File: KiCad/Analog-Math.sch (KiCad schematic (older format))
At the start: 13 parts, among them Q19 2N3904

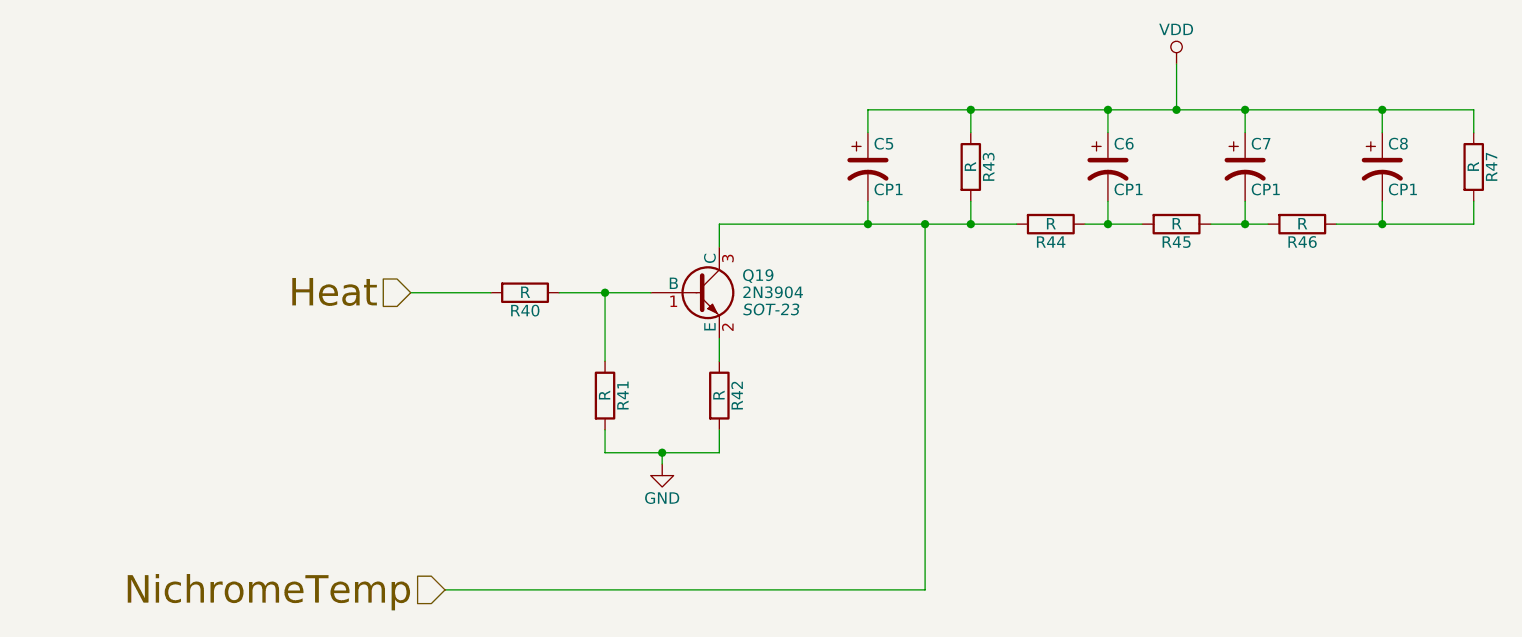
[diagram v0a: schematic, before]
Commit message: HeatOn fix, replaced R1-8 with array
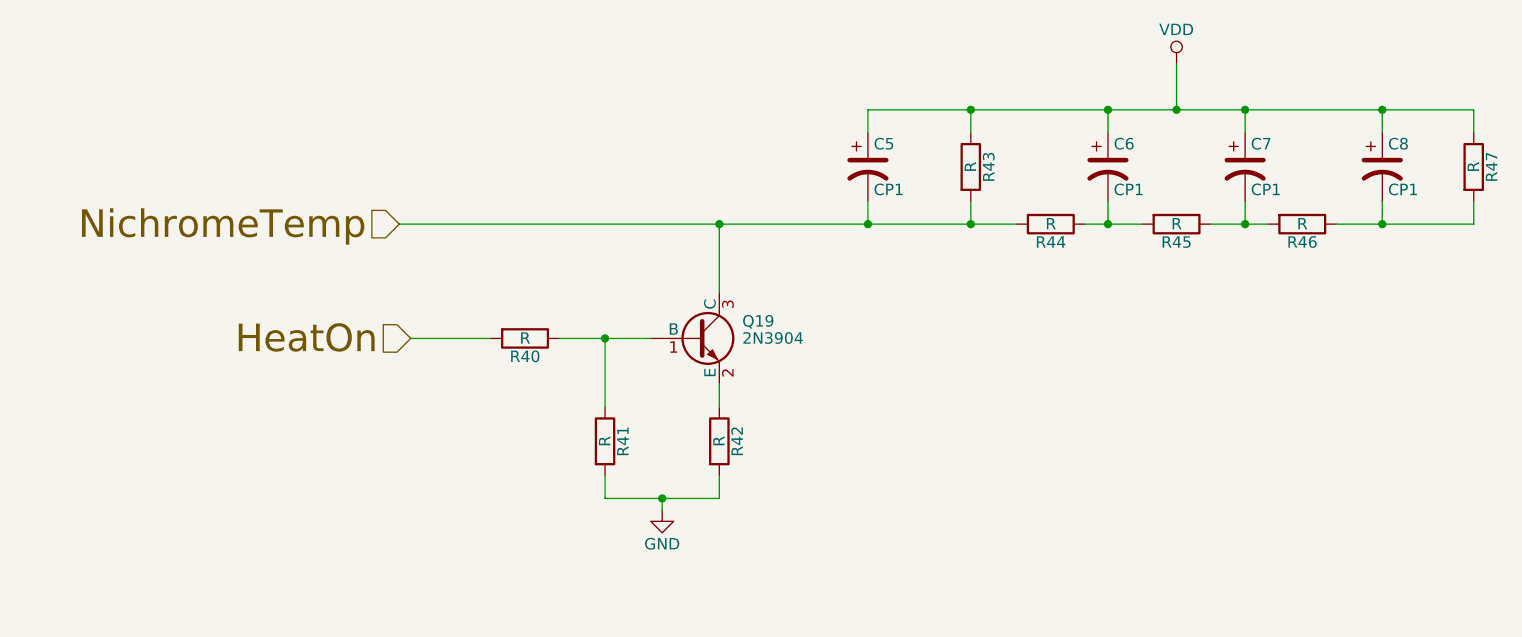
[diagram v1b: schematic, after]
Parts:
- Q19: footprint SOT-23 -> (none)
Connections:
- net Heat renamed HeatOn
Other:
- moved on the sheet: Q19, R40, R41, R42
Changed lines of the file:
@@
 Comment4 ""
 $EndDescr
-Text HLabel 3000 4200 0    120  Input ~ 0
+Text HLabel 2800 2600 0    120  Input ~ 0
 NichromeTemp
-Text HLabel 2850 2900 0    120  Input ~ 0
-Heat
+Text HLabel 2850 3100 0    120  Input ~ 0
+HeatOn
 $Comp
 L MMBT3904 Q19
 U 1 1 5683E9CB
-P 4100 2900
-F 0 "Q19" H 4300 2975 50  0000 L CNN
-F 1 "2N3904" H 4300 2900 50  0000 L CNN
-F 2 "SOT-23" H 4300 2825 50  0000 L CIN
-F 3 "" H 4100 2900 50  0000 L CNN
-	1    4100 2900
+P 4100 3100
+F 0 "Q19" H 4300 3175 50  0000 L CNN
+F 1 "2N3904" H 4300 3100 50  0000 L CNN
+F 2 "" H 4300 3025 50  0001 L CIN
+F 3 "" H 4100 3100 50  0000 L CNN
+	1    4100 3100
 	1    0    0    -1
 $EndComp
@@
 L R R40
 U 1 1 5683EA71
-P 3350 2900
-F 0 "R40" V 3430 2900 50  0000 C CNN
-F 1 "R" V 3350 2900 50  0000 C CNN
-F 2 "" V 3280 2900 50  0000 C CNN
-F 3 "" H 3350 2900 50  0000 C CNN
-	1    3350 2900
+P 3350 3100
+F 0 "R40" V 3430 3100 50  0000 C CNN
+F 1 "R" V 3350 3100 50  0000 C CNN
+F 2 "" V 3280 3100 50  0001 C CNN
+F 3 "" H 3350 3100 50  0000 C CNN
+	1    3350 3100
 	0    1    1    0
 $EndComp
@@
 L R R41
 U 1 1 5683EABC
-P 3700 3350
-F 0 "R41" V 3780 3350 50  0000 C CNN
-F 1 "R" V 3700 3350 50  0000 C CNN
-F 2 "" V 3630 3350 50  0000 C CNN
-F 3 "" H 3700 3350 50  0000 C CNN
-	1    3700 3350
+P 3700 3550
+F 0 "R41" V 3780 3550 50  0000 C CNN
+F 1 "R" V 3700 3550 50  0000 C CNN
+F 2 "" V 3630 3550 50  0001 C CNN
+F 3 "" H 3700 3550 50  0000 C CNN
+	1    3700 3550
 	1    0    0    -1
 $EndComp
@@
 L R R42
 U 1 1 5683ED88
-P 4200 3350
-F 0 "R42" V 4280 3350 50  0000 C CNN
-F 1 "R" V 4200 3350 50  0000 C CNN
-F 2 "" V 4130 3350 50  0000 C CNN
-F 3 "" H 4200 3350 50  0000 C CNN
-	1    4200 3350
-	1    0    0    -1
-$EndComp
-$Comp
-L GND #PWR48
+P 4200 3550
+F 0 "R42" V 4280 3550 50  0000 C CNN
+F 1 "R" V 4200 3550 50  0000 C CNN
+F 2 "" V 4130 3550 50  0001 C CNN
+F 3 "" H 4200 3550 50  0000 C CNN
+	1    4200 3550
+	1    0    0    -1
+$EndComp
+$Comp
+L GND #PWR048
 U 1 1 5683EDA5
-P 3950 3650
-F 0 "#PWR48" H 3950 3400 50  0001 C CNN
-F 1 "GND" H 3950 3500 50  0000 C CNN
-F 2 "" H 3950 3650 50  0000 C CNN
-F 3 "" H 3950 3650 50  0000 C CNN
-	1    3950 3650
+P 3950 3850
+F 0 "#PWR048" H 3950 3600 50  0001 C CNN
+F 1 "GND" H 3950 3700 50  0000 C CNN
+F 2 "" H 3950 3850 50  0000 C CNN
+F 3 "" H 3950 3850 50  0000 C CNN
+	1    3950 3850
 	1    0    0    -1
 $EndComp
@@
 F 0 "C5" H 4875 2450 50  0000 L CNN
 F 1 "CP1" H 4875 2250 50  0000 L CNN
-F 2 "" H 4850 2350 50  0000 C CNN
+F 2 "" H 4850 2350 50  0001 C CNN
 F 3 "" H 4850 2350 50  0000 C CNN
 	1    4850 2350
@@
 $EndComp
 $Comp
-L VDD #PWR49
+L VDD #PWR049
 U 1 1 5683F0D4
 P 6200 1900
-F 0 "#PWR49" H 6200 1750 50  0001 C CNN
+F 0 "#PWR049" H 6200 1750 50  0001 C CNN
 F 1 "VDD" H 6200 2050 50  0000 C CNN
 F 2 "" H 6200 1900 50  0000 C CNN
@@
 $EndComp
 Wire Wire Line
-	2850 2900 3200 2900
-Wire Wire Line
-	3500 2900 3900 2900
-Wire Wire Line
-	3700 2900 3700 3200
-Connection ~ 3700 2900
-Wire Wire Line
-	3700 3500 3700 3600
-Wire Wire Line
-	3700 3600 4200 3600
-Wire Wire Line
-	4200 3600 4200 3500
-Wire Wire Line
-	4200 3200 4200 3100
-Wire Wire Line
-	3950 3650 3950 3600
-Connection ~ 3950 3600
-Wire Wire Line
-	4200 2700 4200 2600
+	2850 3100 3200 3100
+Wire Wire Line
+	3500 3100 3900 3100
+Wire Wire Line
+	3700 3100 3700 3400
+Connection ~ 3700 3100
+Wire Wire Line
+	3700 3700 3700 3800
+Wire Wire Line
+	3700 3800 4200 3800
+Wire Wire Line
+	4200 3800 4200 3700
+Wire Wire Line
+	4200 3400 4200 3300
+Wire Wire Line
+	3950 3850 3950 3800
+Connection ~ 3950 3800
+Wire Wire Line
+	4200 2600 4200 2900
 Wire Wire Line
 	4850 2600 4850 2500
@@
 F 0 "R43" V 5380 2350 50  0000 C CNN
 F 1 "R" V 5300 2350 50  0000 C CNN
-F 2 "" V 5230 2350 50  0000 C CNN
+F 2 "" V 5230 2350 50  0001 C CNN
 F 3 "" H 5300 2350 50  0000 C CNN
 	1    5300 2350
@@
 F 0 "R44" V 5730 2600 50  0000 C CNN
 F 1 "R" V 5650 2600 50  0000 C CNN
-F 2 "" V 5580 2600 50  0000 C CNN
+F 2 "" V 5580 2600 50  0001 C CNN
 F 3 "" H 5650 2600 50  0000 C CNN
 	1    5650 2600
@@
 F 0 "R46" V 6830 2600 50  0000 C CNN
 F 1 "R" V 6750 2600 50  0000 C CNN
-F 2 "" V 6680 2600 50  0000 C CNN
+F 2 "" V 6680 2600 50  0001 C CNN
 F 3 "" H 6750 2600 50  0000 C CNN
 	1    6750 2600
@@
 F 0 "C8" H 7125 2450 50  0000 L CNN
 F 1 "CP1" H 7125 2250 50  0000 L CNN
-F 2 "" H 7100 2350 50  0000 C CNN
+F 2 "" H 7100 2350 50  0001 C CNN
 F 3 "" H 7100 2350 50  0000 C CNN
 	1    7100 2350
@@
 F 0 "R47" V 7580 2350 50  0000 C CNN
 F 1 "R" V 7500 2350 50  0000 C CNN
-F 2 "" V 7430 2350 50  0000 C CNN
+F 2 "" V 7430 2350 50  0001 C CNN
 F 3 "" H 7500 2350 50  0000 C CNN
 	1    7500 2350
@@
 	6200 1900 6200 2100
 Connection ~ 6200 2100
-Wire Wire Line
-	5100 2600 5100 4200
-Wire Wire Line
-	5100 4200 3000 4200
 $Comp
 L R R45
@@
 F 0 "R45" V 6280 2600 50  0000 C CNN
 F 1 "R" V 6200 2600 50  0000 C CNN
-F 2 "" V 6130 2600 50  0000 C CNN
+F 2 "" V 6130 2600 50  0001 C CNN
 F 3 "" H 6200 2600 50  0000 C CNN
 	1    6200 2600
@@
 F 0 "C6" H 5925 2450 50  0000 L CNN
 F 1 "CP1" H 5925 2250 50  0000 L CNN
-F 2 "" H 5900 2350 50  0000 C CNN
+F 2 "" H 5900 2350 50  0001 C CNN
 F 3 "" H 5900 2350 50  0000 C CNN
 	1    5900 2350
@@
 F 0 "C7" H 6525 2450 50  0000 L CNN
 F 1 "CP1" H 6525 2250 50  0000 L CNN
-F 2 "" H 6500 2350 50  0000 C CNN
+F 2 "" H 6500 2350 50  0001 C CNN
 F 3 "" H 6500 2350 50  0000 C CNN
 	1    6500 2350
@@
 $EndComp
 Wire Wire Line
-	4200 2600 5500 2600
-Connection ~ 5100 2600
+	2800 2600 5500 2600
 Connection ~ 5300 2600
 Wire Wire Line
@@
 Connection ~ 7100 2600
 Connection ~ 4850 2600
+Connection ~ 4200 2600
 $EndSCHEMATC

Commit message: kicad resistor package associations complete
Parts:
- R40, R41, R42, R43, R44, R45, R46, R47: footprint (none) -> Resistors_ThroughHole:Resistor_Horizontal_RM10mm
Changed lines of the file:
@@
 F 0 "R40" V 3430 3100 50  0000 C CNN
 F 1 "R" V 3350 3100 50  0000 C CNN
-F 2 "" V 3280 3100 50  0001 C CNN
+F 2 "Resistors_ThroughHole:Resistor_Horizontal_RM10mm" V 3280 3100 50  0001 C CNN
 F 3 "" H 3350 3100 50  0000 C CNN
 	1    3350 3100
@@
 F 0 "R41" V 3780 3550 50  0000 C CNN
 F 1 "R" V 3700 3550 50  0000 C CNN
-F 2 "" V 3630 3550 50  0001 C CNN
+F 2 "Resistors_ThroughHole:Resistor_Horizontal_RM10mm" V 3630 3550 50  0001 C CNN
 F 3 "" H 3700 3550 50  0000 C CNN
 	1    3700 3550
@@
 F 0 "R42" V 4280 3550 50  0000 C CNN
 F 1 "R" V 4200 3550 50  0000 C CNN
-F 2 "" V 4130 3550 50  0001 C CNN
+F 2 "Resistors_ThroughHole:Resistor_Horizontal_RM10mm" V 4130 3550 50  0001 C CNN
 F 3 "" H 4200 3550 50  0000 C CNN
 	1    4200 3550
@@
 F 0 "R43" V 5380 2350 50  0000 C CNN
 F 1 "R" V 5300 2350 50  0000 C CNN
-F 2 "" V 5230 2350 50  0001 C CNN
+F 2 "Resistors_ThroughHole:Resistor_Horizontal_RM10mm" V 5230 2350 50  0001 C CNN
 F 3 "" H 5300 2350 50  0000 C CNN
 	1    5300 2350
@@
 F 0 "R44" V 5730 2600 50  0000 C CNN
 F 1 "R" V 5650 2600 50  0000 C CNN
-F 2 "" V 5580 2600 50  0001 C CNN
+F 2 "Resistors_ThroughHole:Resistor_Horizontal_RM10mm" V 5580 2600 50  0001 C CNN
 F 3 "" H 5650 2600 50  0000 C CNN
 	1    5650 2600
@@
 F 0 "R46" V 6830 2600 50  0000 C CNN
 F 1 "R" V 6750 2600 50  0000 C CNN
-F 2 "" V 6680 2600 50  0001 C CNN
+F 2 "Resistors_ThroughHole:Resistor_Horizontal_RM10mm" V 6680 2600 50  0001 C CNN
 F 3 "" H 6750 2600 50  0000 C CNN
 	1    6750 2600
@@
 F 0 "R47" V 7580 2350 50  0000 C CNN
 F 1 "R" V 7500 2350 50  0000 C CNN
-F 2 "" V 7430 2350 50  0001 C CNN
+F 2 "Resistors_ThroughHole:Resistor_Horizontal_RM10mm" V 7430 2350 50  0001 C CNN
 F 3 "" H 7500 2350 50  0000 C CNN
 	1    7500 2350
@@
 F 0 "R45" V 6280 2600 50  0000 C CNN
 F 1 "R" V 6200 2600 50  0000 C CNN
-F 2 "" V 6130 2600 50  0001 C CNN
+F 2 "Resistors_ThroughHole:Resistor_Horizontal_RM10mm" V 6130 2600 50  0001 C CNN
 F 3 "" H 6200 2600 50  0000 C CNN
 	1    6200 2600

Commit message: capacitors and diode part associations
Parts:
- C5, C6, C7, C8: footprint (none) -> Capacitors_ThroughHole:C_Disc_D6_P5
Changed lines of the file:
@@
 F 0 "C5" H 4875 2450 50  0000 L CNN
 F 1 "CP1" H 4875 2250 50  0000 L CNN
-F 2 "" H 4850 2350 50  0001 C CNN
+F 2 "Capacitors_ThroughHole:C_Disc_D6_P5" H 4850 2350 50  0001 C CNN
 F 3 "" H 4850 2350 50  0000 C CNN
 	1    4850 2350
@@
 F 0 "C8" H 7125 2450 50  0000 L CNN
 F 1 "CP1" H 7125 2250 50  0000 L CNN
-F 2 "" H 7100 2350 50  0001 C CNN
+F 2 "Capacitors_ThroughHole:C_Disc_D6_P5" H 7100 2350 50  0001 C CNN
 F 3 "" H 7100 2350 50  0000 C CNN
 	1    7100 2350
@@
 F 0 "C6" H 5925 2450 50  0000 L CNN
 F 1 "CP1" H 5925 2250 50  0000 L CNN
-F 2 "" H 5900 2350 50  0001 C CNN
+F 2 "Capacitors_ThroughHole:C_Disc_D6_P5" H 5900 2350 50  0001 C CNN
 F 3 "" H 5900 2350 50  0000 C CNN
 	1    5900 2350
@@
 F 0 "C7" H 6525 2450 50  0000 L CNN
 F 1 "CP1" H 6525 2250 50  0000 L CNN
-F 2 "" H 6500 2350 50  0001 C CNN
+F 2 "Capacitors_ThroughHole:C_Disc_D6_P5" H 6500 2350 50  0001 C CNN
 F 3 "" H 6500 2350 50  0000 C CNN
 	1    6500 2350

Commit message: IC BOM and footprints complete
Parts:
- removed Q19: 2N3904, symbol MMBT3904
- added Q19: 2N3904, Easy-PCB-footprints:TO-92, symbol 2N3904
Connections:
- net NichromeTemp: now also Q19.3 (C)
- net at R40.1, R41.1: now also Q19.2 (B)
- net at R42.1: now also Q19.1 (E)
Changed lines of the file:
@@
 HeatOn
-$Comp
-L MMBT3904 Q19
-U 1 1 5683E9CB
-P 4100 3100
-F 0 "Q19" H 4300 3175 50  0000 L CNN
-F 1 "2N3904" H 4300 3100 50  0000 L CNN
-F 2 "" H 4300 3025 50  0001 L CIN
-F 3 "" H 4100 3100 50  0000 L CNN
-	1    4100 3100
-	1    0    0    -1
-$EndComp
 $Comp
 L R R40
@@
 Connection ~ 4850 2600
 Connection ~ 4200 2600
+$Comp
+L 2N3904 Q19
+U 1 1 56882825
+P 4100 3100
+F 0 "Q19" H 4300 3175 50  0000 L CNN
+F 1 "2N3904" H 4300 3100 50  0000 L CNN
+F 2 "Easy-PCB-footprints:TO-92" H 4300 3025 50  0000 L CIN
+F 3 "" H 4100 3100 50  0000 L CNN
+	1    4100 3100
+	1    0    0    -1
+$EndComp
 $EndSCHEMATC

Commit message: errors cleared and components on board
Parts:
- C5, C6, C7, C8: footprint Capacitors_ThroughHole:C_Disc_D6_P5 -> Easy-PCB-footprints:C_Disc_D6_P5
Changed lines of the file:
@@
 F 0 "C5" H 4875 2450 50  0000 L CNN
 F 1 "CP1" H 4875 2250 50  0000 L CNN
-F 2 "Capacitors_ThroughHole:C_Disc_D6_P5" H 4850 2350 50  0001 C CNN
+F 2 "Easy-PCB-footprints:C_Disc_D6_P5" H 4850 2350 50  0001 C CNN
 F 3 "" H 4850 2350 50  0000 C CNN
 	1    4850 2350
@@
 F 0 "C8" H 7125 2450 50  0000 L CNN
 F 1 "CP1" H 7125 2250 50  0000 L CNN
-F 2 "Capacitors_ThroughHole:C_Disc_D6_P5" H 7100 2350 50  0001 C CNN
+F 2 "Easy-PCB-footprints:C_Disc_D6_P5" H 7100 2350 50  0001 C CNN
 F 3 "" H 7100 2350 50  0000 C CNN
 	1    7100 2350
@@
 F 0 "C6" H 5925 2450 50  0000 L CNN
 F 1 "CP1" H 5925 2250 50  0000 L CNN
-F 2 "Capacitors_ThroughHole:C_Disc_D6_P5" H 5900 2350 50  0001 C CNN
+F 2 "Easy-PCB-footprints:C_Disc_D6_P5" H 5900 2350 50  0001 C CNN
 F 3 "" H 5900 2350 50  0000 C CNN
 	1    5900 2350
@@
 F 0 "C7" H 6525 2450 50  0000 L CNN
 F 1 "CP1" H 6525 2250 50  0000 L CNN
-F 2 "Capacitors_ThroughHole:C_Disc_D6_P5" H 6500 2350 50  0001 C CNN
+F 2 "Easy-PCB-footprints:C_Disc_D6_P5" H 6500 2350 50  0001 C CNN
 F 3 "" H 6500 2350 50  0000 C CNN
 	1    6500 2350
